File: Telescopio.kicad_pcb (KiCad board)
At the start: 2 copper layers, 110.7 x 60.5 mm, 10 parts, among them J1 ScaleL, J2 Scale, J3 CONN_01X04, P4 CONN_01X18, P5 CONN_01X18

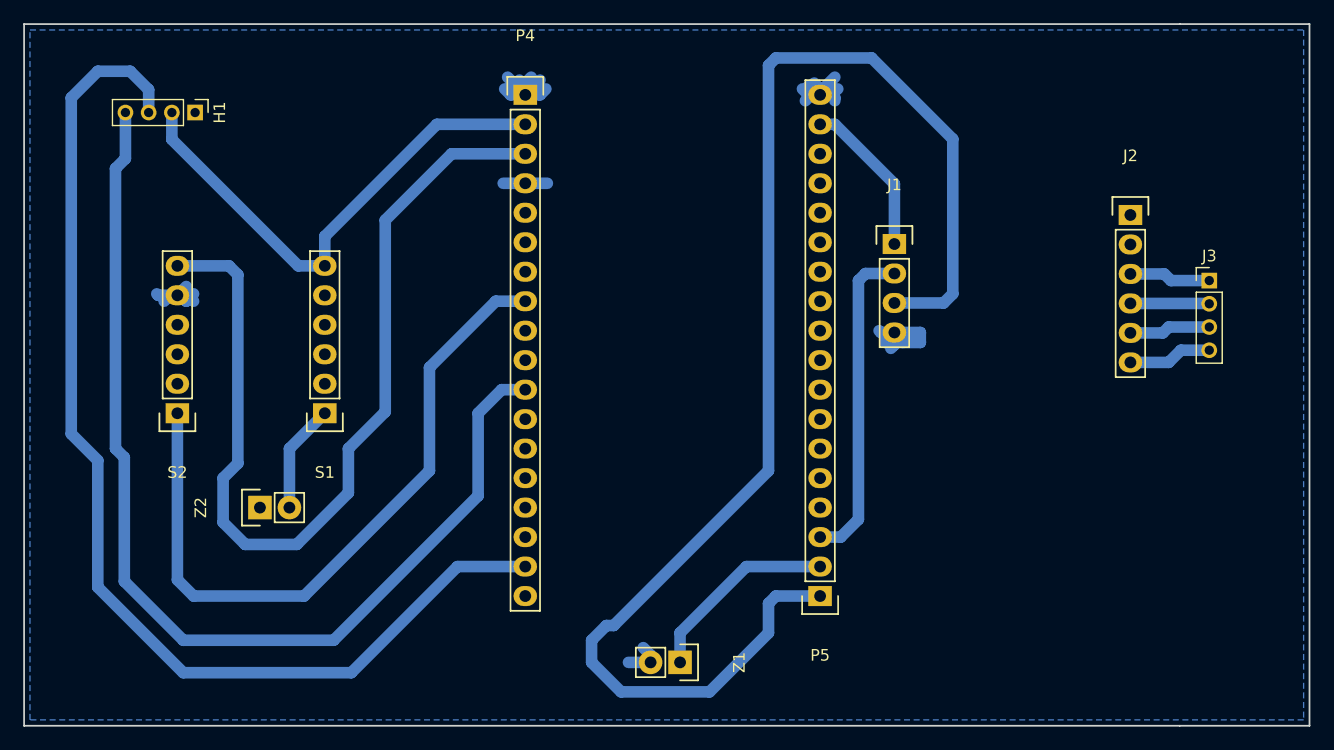
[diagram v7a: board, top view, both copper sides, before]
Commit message: add pinheaders 2.0mm
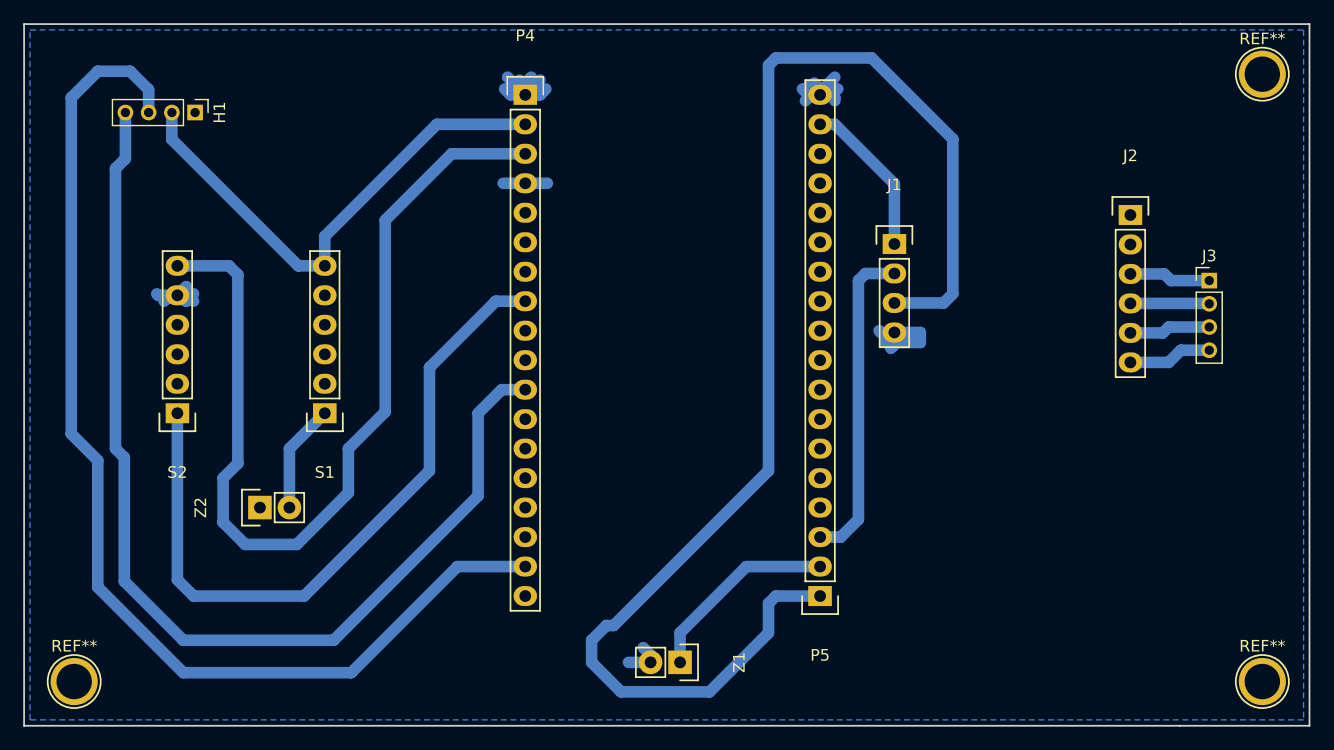
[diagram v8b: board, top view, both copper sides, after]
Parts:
- added REF**: 1pin, Connect:1pin, F.Cu at (198.1, 54.1)
- added REF**: 1pin, Connect:1pin, F.Cu at (198.1, 106.4)
- added REF**: 1pin, Connect:1pin, F.Cu at (95.8, 106.4)
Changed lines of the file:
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@@
     (area 91.364999 49.708999 202.259001 110.311001)
     (thickness 1.6)
-    (drawings 6)
+    (drawings 7)
     (tracks 148)
     (zones 0)
-    (modules 10)
+    (modules 13)
     (nets 16)
   )
@@
   )
   (setup
-    (last_trace_width 1)
+    (last_trace_width 0.25)
     (user_trace_width 0.5)
     (user_trace_width 1)
@@
       (outputformat 1)
       (mirror false)
-      (drillshape 1)
+      (drillshape 0)
       (scaleselection 1)
       (outputdirectory ""))
@@
     )
   )
+  (module Connect:1pin (layer F.Cu)
+    (at 198.12 54.102)
+    (descr "module 1 pin (ou trou mecanique de percage)")
+    (tags DEV)
+    (fp_text reference REF** (at 0 -3.048) (layer F.SilkS)
+      (effects (font (size 1 1) (thickness 0.15)))
+    )
+    (fp_text value 1pin (at 0 2.794) (layer F.Fab)
+      (effects (font (size 1 1) (thickness 0.15)))
+    )
+    (fp_circle (center 0 0) (end 0 -2.286) (layer F.SilkS) (width 0.15))
+    (pad 1 thru_hole circle (at 0 0) (size 4.064 4.064) (drill 3.048) (layers *.Cu *.Mask F.SilkS))
+  )
+  (module Connect:1pin (layer F.Cu)
+    (at 198.12 106.426)
+    (descr "module 1 pin (ou trou mecanique de percage)")
+    (tags DEV)
+    (fp_text reference REF** (at 0 -3.048) (layer F.SilkS)
+      (effects (font (size 1 1) (thickness 0.15)))
+    )
+    (fp_text value 1pin (at 0 2.794) (layer F.Fab)
+      (effects (font (size 1 1) (thickness 0.15)))
+    )
+    (fp_circle (center 0 0) (end 0 -2.286) (layer F.SilkS) (width 0.15))
+    (pad 1 thru_hole circle (at 0 0) (size 4.064 4.064) (drill 3.048) (layers *.Cu *.Mask F.SilkS))
+  )
+  (module Connect:1pin (layer F.Cu)
+    (at 95.758 106.426)
+    (descr "module 1 pin (ou trou mecanique de percage)")
+    (tags DEV)
+    (fp_text reference REF** (at 0 -3.048) (layer F.SilkS)
+      (effects (font (size 1 1) (thickness 0.15)))
+    )
+    (fp_text value 1pin (at 0 2.794) (layer F.Fab)
+      (effects (font (size 1 1) (thickness 0.15)))
+    )
+    (fp_circle (center 0 0) (end 0 -2.286) (layer F.SilkS) (width 0.15))
+    (pad 1 thru_hole circle (at 0 0) (size 4.064 4.064) (drill 3.048) (layers *.Cu *.Mask F.SilkS))
+  )
+  (gr_line (start 198.628 112.776) (end 198.628 112.522) (angle 90) (layer Dwgs.User) (width 0.2))
   (gr_line (start 202.184 110.236) (end 191.008 110.236) (angle 90) (layer Edge.Cuts) (width 0.15))
   (gr_line (start 202.184 49.784) (end 202.184 110.236) (angle 90) (layer Edge.Cuts) (width 0.15))
@@
   (segment (start 170.6626 73.8124) (end 171.45 73.025) (width 1) (layer B.Cu) (net 6))
   (segment (start 166.5732 73.66) (end 166.4208 73.8124) (width 1) (layer B.Cu) (net 6))
-  (segment (start 193.548 71.882) (end 190.246 71.882) (width 1) (layer B.Cu) (net 7) (status 400000))
-  (segment (start 189.6745 71.3105) (end 186.7535 71.3105) (width 1) (layer B.Cu) (net 7) (status 800000))
+  (segment (start 193.548 71.882) (end 190.246 71.882) (width 1) (layer B.Cu) (net 7))
+  (segment (start 189.6745 71.3105) (end 186.7535 71.3105) (width 1) (layer B.Cu) (net 7))
   (segment (start 190.246 71.882) (end 189.6745 71.3105) (width 1) (layer B.Cu) (net 7))
-  (segment (start 186.7535 73.8505) (end 193.5165 73.8505) (width 1) (layer B.Cu) (net 8) (status C00000))
-  (segment (start 193.5165 73.8505) (end 193.548 73.882) (width 1) (layer B.Cu) (net 8) (status C00000))
-  (segment (start 186.7535 76.3905) (end 189.5475 76.3905) (width 1) (layer B.Cu) (net 9) (status 400000))
-  (segment (start 190.056 75.882) (end 193.548 75.882) (width 1) (layer B.Cu) (net 9) (status 800000))
+  (segment (start 186.7535 73.8505) (end 193.5165 73.8505) (width 1) (layer B.Cu) (net 8))
+  (segment (start 193.5165 73.8505) (end 193.548 73.882) (width 1) (layer B.Cu) (net 8))
+  (segment (start 186.7535 76.3905) (end 189.5475 76.3905) (width 1) (layer B.Cu) (net 9))
+  (segment (start 190.056 75.882) (end 193.548 75.882) (width 1) (layer B.Cu) (net 9))
   (segment (start 189.5475 76.3905) (end 190.056 75.882) (width 1) (layer B.Cu) (net 9))
-  (segment (start 186.7535 78.9305) (end 190.0555 78.9305) (width 1) (layer B.Cu) (net 10) (status 400000))
-  (segment (start 191.104 77.882) (end 193.548 77.882) (width 1) (layer B.Cu) (net 10) (status 800000))
+  (segment (start 186.7535 78.9305) (end 190.0555 78.9305) (width 1) (layer B.Cu) (net 10))
+  (segment (start 191.104 77.882) (end 193.548 77.882) (width 1) (layer B.Cu) (net 10))
   (segment (start 190.0555 78.9305) (end 191.104 77.882) (width 1) (layer B.Cu) (net 10))
   (segment (start 104.648 70.612) (end 109.093 70.612) (width 1) (layer B.Cu) (net 11))
